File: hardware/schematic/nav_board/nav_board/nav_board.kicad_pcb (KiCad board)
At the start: 2 copper layers, 118 x 39 mm, 6 parts, among them J1 RS232 to Display, J2 Flow Meter, J3 Depth Sensor

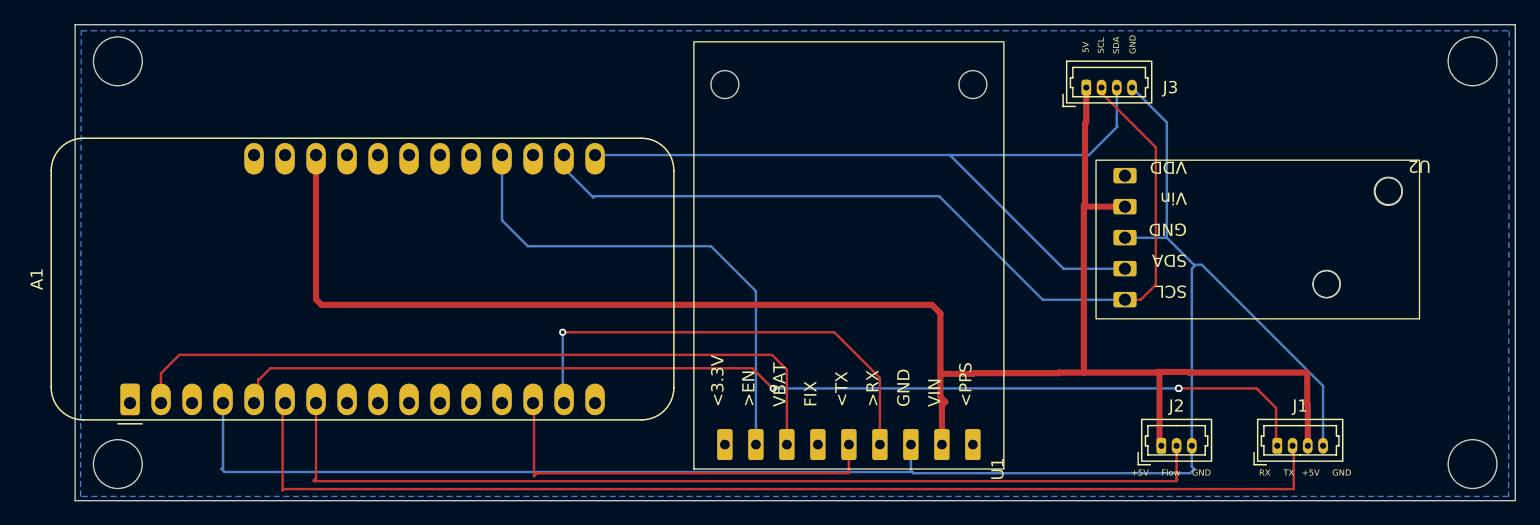
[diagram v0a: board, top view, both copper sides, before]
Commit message: First commit of PCB files for NAV and DISPLAY boards
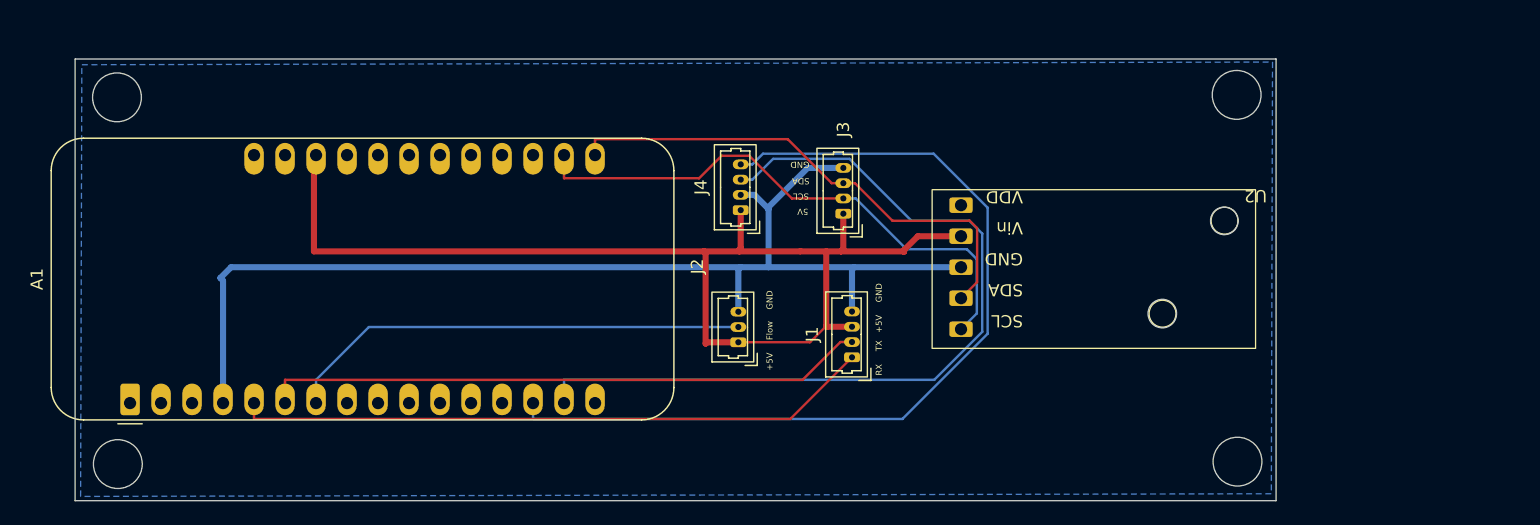
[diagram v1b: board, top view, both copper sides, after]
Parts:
- removed U1: ~, DPVNav Footprint Library:Adafruit Ultimate GPS
- added J4: GPS, Connector_Molex:Molex_PicoBlade_53047-0410_1x04_P1.25mm_Vertical, F.Cu at (80.0, 47.2)
- J1: value RS232 to Display -> Display
- moved J2 35.7 mm to (79.8, 58.0), turned to 90 degrees
- moved J1 35.6 mm to (89.2, 59.2), turned to 90 degrees
- moved J3 22.4 mm to (88.4, 47.5), turned to 90 degrees
- moved U2 13.6 mm to (122.2, 45.5)
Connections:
- A1 pad 2: Net-(A1-3V3) -> unconnected-(A1-3V3-Pad2)
- A1 pad 20: Net-(A1-A7/IO32) -> unconnected-(A1-A7/IO32-Pad20)
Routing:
- net Net-(A1-3V3): track 61.0 -> 0.00 mm
- net GND: track 144.3 -> 93.6 mm
- net +5V: track 143.7 -> 94.5 mm
- net Net-(A1-DAC1/A1): track 93.8 -> 49.6 mm
- net Net-(A1-I34/A2): track 80.1 -> 38.3 mm
- net Net-(A1-A7/IO32): track 41.1 -> 0.00 mm
- net Net-(A1-RX/IO16): track 34.3 -> 74.2 mm
- net Net-(A1-DAC2/A0): track 90.5 -> 52.4 mm, vias 3 -> 0
- net Net-(A1-TX/IO17): track 38.8 -> 68.9 mm, vias 1 -> 0
- net Net-(A1-SCL/IO22): track 72.6 -> 46.3 mm
- net Net-(A1-SDA/IO23): track 65.2 -> 41.9 mm
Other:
- board size 118 x 39 mm -> 98.4 x 36.2 mm
